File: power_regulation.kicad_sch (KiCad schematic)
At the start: 8 parts, among them J4 171856-0002, J6 171856-0002, U1 NCP1117LPST33T3G

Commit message: Cleanup symbol field table
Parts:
- C1, C2: ALTIUM_VALUE 10uF -> (none); CAPACITANCE 10uF -> (none); CASE CODE (IMPERIAL) 1206 -> (none); CASE CODE (METRIC) 3216 -> (none); CASE/PACKAGE 1206 -> (none); DEPTH 1.6mm -> (none); DIELECTRIC MATERIAL Tantalum -> (none); DISSIPATION FACTOR 8% -> (none); ESR (EQUIVALENT SERIES RESISTANCE) 3R -> (none); FEATURES General Purpose -> (none); HEIGHT 1.6mm -> (none); HEIGHT - SEATED (MAX) 0.071inch -> (none); LEAD FREE Lead Free -> (none); LEAD PITCH 1.1mm -> (none); LEAKAGE CURRENT 1.6uA -> (none); LENGTH 3.2mm -> (none); MANUFACTURER KYOCERA AVX -> (none); MANUFACTURER PART NUMBER TAJA106K016RNJ -> (none); MAX OPERATING TEMPERATURE 125°C -> (none); MIN OPERATING TEMPERATURE -55°C -> (none); MOUNT Surface Mount -> (none); NUMBER OF PINS 2 -> (none); PACKAGE QUANTITY 1 -> (none); PACKAGING Tape and Reel -> (none); POLARITY Polar -> (none); Part Number (none) -> TAJA106K016RNJ; RADIATION HARDENING No -> (none); REACH SVHC No SVHC -> (none); TERMINATION SMD/SMT -> (none); TOLERANCE 10% -> (none); VOLTAGE 16V -> (none); VOLTAGE RATING 16V -> (none); VOLTAGE RATING (DC) 16V -> (none); WIDTH 1.6mm -> (none)
- F1: ALTIUM_VALUE 2A -> (none); APPROVALS UL -> (none); CASE CODE (IMPERIAL) 1206 -> (none); CASE CODE (METRIC) 3216 -> (none); CASE/PACKAGE 1206 -> (none); CURRENT 2A -> (none); CURRENT RATING 2A -> (none); DC COLD RESISTANCE 31mR -> (none); DEPTH 1.52mm -> (none); FUSE TYPE Board Mount (Cartridge Style Excluded) -> (none); HEIGHT 0.023inch -> (none); HOUSING MATERIAL Ceramic -> (none); LENGTH 3.18mm -> (none); MANUFACTURER Littelfuse Inc. -> (none); MANUFACTURER PART NUMBER 0466002.NRHF -> (none); MAX OPERATING TEMPERATURE 90°C -> (none); MIN OPERATING TEMPERATURE -55°C -> (none); MOUNT Surface Mount -> (none); PACKAGE QUANTITY 5000 -> (none); PACKAGING Tape and Reel -> (none); POWER DISSIPATION 157.5mW -> (none); Part Number (none) -> 0466002.NRHF; VOLTAGE RATING (AC) 63V -> (none); VOLTAGE RATING (DC) 63V -> (none); WIDTH 0.06inch -> (none)
- F2: ALTIUM_VALUE 1A -> (none); AUTOMOTIVE No -> (none); CATEGORY Fuse -> (none); COMPONENTLINK2DESCRIPTION Datasheet -> (none); COMPONENTLINK2URL https://www.littelfuse.com/~/media/electronics/datasheets/f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 -> (none); DEVICE CLASS L1 Circuit Protection -> (none); DEVICE CLASS L2 Fuses -> (none); DEVICE CLASS L3 unset -> (none); DIGIKEY DESCRIPTION FUSE BOARD MNT 1A 63VAC/VDC 1206 -> (none); FUSE BLOW SPEED Fast -> (none); FUSE CURRENT 1A -> (none); FUSE I2T 0.0423A2Sec -> (none); FUSE INTERRUPT AC CURRENT 50A -> (none); FUSE INTERRUPT DC CURRENT 50A -> (none); FUSE VOLTAGE DROP 79.97mV -> (none); HEIGHT 0.66mm -> (none); LEAD FREE Yes -> (none); MANUFACTURER Littelfuse Inc -> (none); MANUFACTURER PART NUMBER 0466001.NR -> (none); MAX FUSE AC VOLTAGE 63V -> (none); MAX FUSE DC VOLTAGE 63V -> (none); MOUSER DESCRIPTION Surface Mount Fuses 63V FA 1206 1A VFA Slimline -> (none); OCTOPART https://octopart.com/0466001.nr-littelfuse-566005 -> (none); PACKAGE 0466 -> (none); Part Number (none) -> 0466001.NR; RESISTANCE 0.075Ω -> (none); ROHS TRUE -> (none); TEMPERATURE -55°C to +90°C -> (none); TEMPERATURE RANGE HIGH +90°C -> (none); TEMPERATURE RANGE LOW -55°C -> (none); VOLTAGE RATING 63V -> (none)
- J4, J6: ALTIUM_VALUE 1x2 -> (none); DATASHEET LINK https://componentsearchengine.com//171856-0002.pdf -> (none); HEIGHT 8.18mm -> (none); MANUFACTURER Molex -> (none); MANUFACTURER PART NUMBER 171856-0002 -> (none); MANUFACTURER_NAME Molex -> (none); MOUSER2 PART NUMBER 538-171856-0002 -> (none); MOUSER2 PRICE/STOCK https://www.mouser.com/Search/Refine.aspx?Keyword=538-17185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 -> (none); Part Number (none) -> 171856-0002
- R7: @ QTY 1500 -> (none); ALTIUM_VALUE 0.0 -> (none); COMPOSITION Thick Film -> (none); DATASHEETS http://industrial.panasonic.com/www-cgi/jvcr13pz.cgi?E+PZ+3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 -> (none); DIGI-KEY PART NUMBER P0.0ACT-ND -> (none); FACTORY STOCK 0 -> (none); FAILURE RATE - -> (none); FEATURES Automotive AEC-Q200 -> (none); HEIGHT - SEATED (MAX) 0.028" (0.70mm) -> (none); IMAGE //media.digikey.com/Renders/Panasonic%20Renders/ERJ-0805%20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 -> (none); MANUFACTURER Panasonic Electronic Components -> (none); MANUFACTURER PART NUMBER ERJ-6GEY0R00V -> (none); MINIMUM QUANTITY 1 -> (none); NUMBER OF TERMINATIONS 2 -> (none); OPERATING TEMPERATURE -55°C ~ 155°C -> (none); PACKAGE / CASE 0805 (2012 Metric) -> (none); PACKAGING Cut Tape (CT) -> (none); PART NUMBER ERJ-6GEY0R00V -> (none); PART STATUS Active -> (none); POWER (WATTS) 0.125W, 1/8W -> (none); Part Number (none) -> ERJ-6GEY0R00V; QUANTITY AVAILABLE 1597627 -> (none); SERIES ERJ -> (none); SIZE / DIMENSION 0.079" L x 0.049" W (2.00mm x 1.25mm) -> (none); SUPPLIER DEVICE PACKAGE 0805 -> (none); TEMPERATURE COEFFICIENT - -> (none); TOLERANCE Jumper -> (none); UNIT PRICE (USD) 0.00544 -> (none)
- U1: ALTIUM_VALUE 1A -> (none); CASE/PACKAGE SOT-223 -> (none); CONTACT PLATING Tin -> (none); DROPOUT VOLTAGE 1.3V -> (none); HALOGEN FREE Halogen Free -> (none); HEIGHT 1.69mm -> (none); LEAD FREE Lead Free -> (none); LENGTH 6.7mm -> (none); MANUFACTURER On Semiconductor -> (none); MANUFACTURER PART NUMBER NCP1117LPST33T3G -> (none); MAX INPUT VOLTAGE 18V -> (none); MAX OPERATING TEMPERATURE 125°C -> (none); MAX OUTPUT CURRENT 1A -> (none); MIN CURRENT LIMIT 1.1A -> (none); MIN INPUT VOLTAGE -300mV -> (none); MIN OPERATING TEMPERATURE 0°C -> (none); MIN OUTPUT VOLTAGE 3.3V -> (none); MOUNT Surface Mount -> (none); NOMINAL OUTPUT VOLTAGE 3.3V -> (none); NUMBER OF OUTPUTS 1 -> (none); NUMBER OF PINS 3 -> (none); NUMBER OF REGULATORS 1 -> (none); OUTPUT CURRENT 1A -> (none); OUTPUT TYPE Fixed -> (none); OUTPUT VOLTAGE 3.3V -> (none); PACKAGE QUANTITY 1 -> (none); PACKAGING Tape and Reel -> (none); POLARITY Positive -> (none); POWER SUPPLY REJECTION RATIO (PSRR) 60dB -> (none); Part Number (none) -> NCP1117LPST33T3G; QUIESCENT CURRENT 700uA -> (none); REACH SVHC No SVHC -> (none); REFERENCE VOLTAGE 1.275V -> (none); WIDTH 3.7mm -> (none)

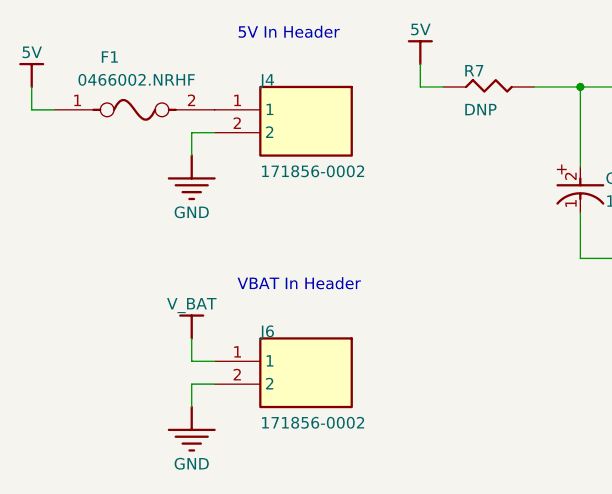
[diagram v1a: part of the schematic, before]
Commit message: Input and Output Header Updates to MEB
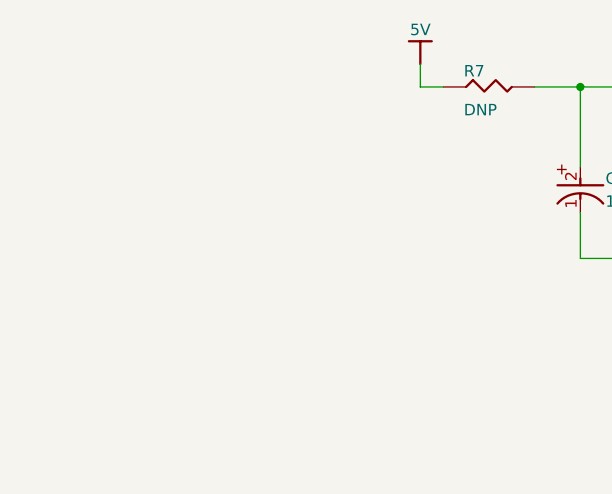
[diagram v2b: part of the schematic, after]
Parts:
- removed F1: 0466002.NRHF, AltiumImport:FP-0466-MFG, symbol MEB-altium-import:power_regulation_0_5bcf9b9f640e542cf0359d10258e979
- removed J4, J6: 171856-0002, AltiumImport:SHDR2W99P0X254_1X2_493X635X818P, symbol MEB-altium-import:power_regulation_0_171856-0002
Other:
- note removed: "5V In Header"
- note removed: "VBAT In Header"
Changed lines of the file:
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@@
   (junction (at 147.32 98.2472) (diameter 0) (color 0 0 0 0)
   )
-  (wire (pts (xy 86.36 100.7872) (xy 88.9 100.7872))
-    (stroke (width 0.254) (type default))
-  )
-  (wire (pts (xy 86.36 98.2472) (xy 86.36 100.7872))
-    (stroke (width 0.254) (type default))
-  )
   (wire (pts (xy 147.32 98.2472) (xy 152.4 98.2472))
     (stroke (width 0.254) (type default))
@@
     (stroke (width 0.254) (type default))
   )
-  (wire (pts (xy 104.14 131.2672) (xy 104.14 133.8072))
-    (stroke (width 0.254) (type default))
-  )
-  (wire (pts (xy 106.68 128.7272) (xy 104.14 128.7272))
-    (stroke (width 0.254) (type default))
-  )
   (wire (pts (xy 210.82 100.7872) (xy 203.2 100.7872))
     (stroke (width 0.254) (type default))
@@
     (stroke (width 0.254) (type default))
   )
-  (wire (pts (xy 106.68 103.3272) (xy 104.14 103.3272))
-    (stroke (width 0.254) (type default))
-  )
   (wire (pts (xy 203.2 117.2972) (xy 203.2 122.3772))
     (stroke (width 0.254) (type default))
@@
     (stroke (width 0.254) (type default))
   )
-  (wire (pts (xy 104.14 103.3272) (xy 104.14 105.8672))
-    (stroke (width 0.254) (type default))
-  )
-  (wire (pts (xy 106.68 131.2672) (xy 104.14 131.2672))
-    (stroke (width 0.254) (type default))
-  )
   (wire (pts (xy 203.2 98.2472) (xy 210.82 98.2472))
     (stroke (width 0.254) (type default))
@@
     (stroke (width 0.254) (type default))
   )
-  (wire (pts (xy 104.14 128.7272) (xy 104.14 126.1872))
-    (stroke (width 0.254) (type default))
-  )
   (wire (pts (xy 210.82 117.2972) (xy 210.82 112.2172))
     (stroke (width 0.254) (type default))
   )
-  (text "5V In Header" (at 109.22 93.1672 0)
-    (effects (font (size 1.27 1.27)) (justify left bottom))
-  )
-  (text "VBAT In Header" (at 109.22 121.1072 0)
-    (effects (font (size 1.27 1.27)) (justify left bottom))
-  )
   (symbol (lib_id "MEB-altium-import:power_regulation_0_ERJ-6GEY0R00V") (at 137.16 98.2472 0) (unit 1)
     (in_bom yes) (on_board yes) (dnp no)
@@
         (path "/228e4997-23c1-4c21-939b-583cad26a5e3/90a8e139-216e-4b02-83ea-4edb1f5f4c15"
           (reference "R7") (unit 1)
-        )
-      )
-    )
-  )
-  (symbol (lib_id "MEB-altium-import:GND") (at 104.14 133.8072 0) (unit 1)
-    (in_bom yes) (on_board yes) (dnp no)
-    (property "Reference" "#PWR0127" (at 104.14 133.8072 0)
-      (effects (font (size 1.27 1.27)) hide)
-    )
-    (property "Value" "GND" (at 104.14 140.1572 0)
-      (effects (font (size 1.27 1.27)))
-    )
-    (property "Footprint" "" (at 104.14 133.8072 0)
-      (effects (font (size 1.27 1.27)) hide)
-    )
-    (property "Datasheet" "" (at 104.14 133.8072 0)
-      (effects (font (size 1.27 1.27)) hide)
-    )
-    (pin "")
-    (instances
-      (project "MEB"
-        (path "/228e4997-23c1-4c21-939b-583cad26a5e3/90a8e139-216e-4b02-83ea-4edb1f5f4c15"
-          (reference "#PWR0127") (unit 1)
-        )
-      )
-    )
-  )
-  (symbol (lib_id "MEB-altium-import:power_regulation_0_171856-0002") (at 106.68 100.7872 0) (unit 1)
-    (in_bom yes) (on_board yes) (dnp no)
-    (property "Reference" "J4" (at 111.76 98.2472 0)
-      (effects (font (size 1.27 1.27)) (justify left bottom))
-    )
-    (property "Value" "171856-0002" (at 111.76 108.4072 0)
-      (effects (font (size 1.27 1.27)) (justify left bottom))
-    )
-    (property "Footprint" "AltiumImport:SHDR2W99P0X254_1X2_493X635X818P" (at 106.68 100.7872 0)
-      (effects (font (size 1.27 1.27)) hide)
-    )
-    (property "Datasheet" "" (at 106.68 100.7872 0)
-      (effects (font (size 1.27 1.27)) hide)
-    )
-    (property "Part Number" "171856-0002" (at 106.68 100.7872 0)
-      (effects (font (size 1.27 1.27)) hide)
-    )
-    (pin "1")
-    (pin "2")
-    (instances
-      (project "MEB"
-        (path "/228e4997-23c1-4c21-939b-583cad26a5e3/90a8e139-216e-4b02-83ea-4edb1f5f4c15"
-          (reference "J4") (unit 1)
-        )
-      )
-    )
-  )
-  (symbol (lib_id "MEB-altium-import:5V") (at 86.36 98.2472 180) (unit 1)
-    (in_bom yes) (on_board yes) (dnp no)
-    (property "Reference" "#PWR0129" (at 86.36 98.2472 0)
-      (effects (font (size 1.27 1.27)) hide)
-    )
-    (property "Value" "5V" (at 86.36 94.4372 0)
-      (effects (font (size 1.27 1.27)))
-    )
-    (property "Footprint" "" (at 86.36 98.2472 0)
-      (effects (font (size 1.27 1.27)) hide)
-    )
-    (property "Datasheet" "" (at 86.36 98.2472 0)
-      (effects (font (size 1.27 1.27)) hide)
-    )
-    (pin "")
-    (instances
-      (project "MEB"
-        (path "/228e4997-23c1-4c21-939b-583cad26a5e3/90a8e139-216e-4b02-83ea-4edb1f5f4c15"
-          (reference "#PWR0129") (unit 1)
         )
       )
@@
     )
   )
-  (symbol (lib_id "MEB-altium-import:power_regulation_0_5bcf9b9f640e542cf0359d10258e979") (at 88.9 100.7872 0) (unit 1)
-    (in_bom yes) (on_board yes) (dnp no)
-    (property "Reference" "F1" (at 93.98 95.7072 0)
-      (effects (font (size 1.27 1.27)) (justify left bottom))
-    )
-    (property "Value" "0466002.NRHF" (at 91.44 98.2472 0)
-      (effects (font (size 1.27 1.27)) (justify left bottom))
-    )
-    (property "Footprint" "AltiumImport:FP-0466-MFG" (at 88.9 100.7872 0)
-      (effects (font (size 1.27 1.27)) hide)
-    )
-    (property "Datasheet" "" (at 88.9 100.7872 0)
-      (effects (font (size 1.27 1.27)) hide)
-    )
-    (property "Part Number" "0466002.NRHF" (at 88.9 100.7872 0)
-      (effects (font (size 1.27 1.27)) hide)
-    )
-    (pin "1")
-    (pin "2")
-    (instances
-      (project "MEB"
-        (path "/228e4997-23c1-4c21-939b-583cad26a5e3/90a8e139-216e-4b02-83ea-4edb1f5f4c15"
-          (reference "F1") (unit 1)
-        )
-      )
-    )
-  )
-  (symbol (lib_id "MEB-altium-import:V_BAT") (at 104.14 126.1872 180) (unit 1)
-    (in_bom yes) (on_board yes) (dnp no)
-    (property "Reference" "#PWR0126" (at 104.14 126.1872 0)
-      (effects (font (size 1.27 1.27)) hide)
-    )
-    (property "Value" "V_BAT" (at 104.14 122.3772 0)
-      (effects (font (size 1.27 1.27)))
-    )
-    (property "Footprint" "" (at 104.14 126.1872 0)
-      (effects (font (size 1.27 1.27)) hide)
-    )
-    (property "Datasheet" "" (at 104.14 126.1872 0)
-      (effects (font (size 1.27 1.27)) hide)
-    )
-    (pin "")
-    (instances
-      (project "MEB"
-        (path "/228e4997-23c1-4c21-939b-583cad26a5e3/90a8e139-216e-4b02-83ea-4edb1f5f4c15"
-          (reference "#PWR0126") (unit 1)
-        )
-      )
-    )
-  )
   (symbol (lib_id "MEB-altium-import:power_regulation_0_ba9dfc6f1948e29eb9591bef83395b3") (at 152.4 98.2472 0) (unit 1)
     (in_bom yes) (on_board yes) (dnp no)
@@
     )
   )
-  (symbol (lib_id "MEB-altium-import:power_regulation_0_171856-0002") (at 106.68 128.7272 0) (unit 1)
-    (in_bom yes) (on_board yes) (dnp no)
-    (property "Reference" "J6" (at 111.76 126.1872 0)
-      (effects (font (size 1.27 1.27)) (justify left bottom))
-    )
-    (property "Value" "171856-0002" (at 111.76 136.3472 0)
-      (effects (font (size 1.27 1.27)) (justify left bottom))
-    )
-    (property "Footprint" "AltiumImport:SHDR2W99P0X254_1X2_493X635X818P" (at 106.68 128.7272 0)
-      (effects (font (size 1.27 1.27)) hide)
-    )
-    (property "Datasheet" "" (at 106.68 128.7272 0)
-      (effects (font (size 1.27 1.27)) hide)
-    )
-    (property "Part Number" "171856-0002" (at 106.68 128.7272 0)
-      (effects (font (size 1.27 1.27)) hide)
-    )
-    (pin "1")
-    (pin "2")
-    (instances
-      (project "MEB"
-        (path "/228e4997-23c1-4c21-939b-583cad26a5e3/90a8e139-216e-4b02-83ea-4edb1f5f4c15"
-          (reference "J6") (unit 1)
-        )
-      )
-    )
-  )
   (symbol (lib_id "MEB-altium-import:power_regulation_0_5bcf9b9f640e542cf0359d10258e979") (at 212.09 98.2472 0) (unit 1)
     (in_bom yes) (on_board yes) (dnp no)
@@
         )
       )
-    )
-  )
-  (symbol (lib_id "MEB-altium-import:GND") (at 104.14 105.8672 0) (unit 1)
-    (in_bom yes) (on_board yes) (dnp no)
-    (property "Reference" "#PWR0130" (at 104.14 105.8672 0)
-      (effects (font (size 1.27 1.27)) hide)
-    )
-    (property "Value" "GND" (at 104.14 112.2172 0)
-      (effects (font (size 1.27 1.27)))
-    )
-    (property "Footprint" "" (at 104.14 105.8672 0)
-      (effects (font (size 1.27 1.27)) hide)
-    )
-    (property "Datasheet" "" (at 104.14 105.8672 0)
-      (effects (font (size 1.27 1.27)) hide)
-    )
-    (pin "")
-    (instances
-      (project "MEB"
-        (path "/228e4997-23c1-4c21-939b-583cad26a5e3/90a8e139-216e-4b02-83ea-4edb1f5f4c15"
-          (reference "#PWR0130") (unit 1)
-        )
-      )

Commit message: Finalized schematic and began assigning footprints
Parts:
- R7: footprint AltiumImport:SMD-0805-RES -> Resistor_SMD:R_0805_2012Metric_Pad1.20x1.40mm_HandSolder
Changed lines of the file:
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@@
       (effects (font (size 1.27 1.27)) (justify left bottom))
     )
-    (property "Footprint" "AltiumImport:SMD-0805-RES" (at 137.16 98.2472 0)
+    (property "Footprint" "Resistor_SMD:R_0805_2012Metric_Pad1.20x1.40mm_HandSolder" (at 137.16 98.2472 0)
       (effects (font (size 1.27 1.27)) hide)
     )
